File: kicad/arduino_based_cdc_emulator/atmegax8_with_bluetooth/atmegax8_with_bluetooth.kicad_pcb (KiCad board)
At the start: 2 copper layers, 110.5 x 172.6 mm, 70 parts, among them IC1 ATMEGA88-A, P1 CONN_9, P2 SPI, P3 CONN_4, Q1 BC817-40, U1 78L05, U2 F-6188, U3 LM358, Y1 Crystal_GND2

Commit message: update
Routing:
- net TX: track 2.51 -> 29.2 mm, vias 0 -> 1
- net RX: track 0.00 -> 23.3 mm, vias 0 -> 1
- net /LED2: track 0.00 -> 15.7 mm, vias 0 -> 2
- net /LED1: track 12.5 -> 17.3 mm, vias 0 -> 2
- net /ARESET: track 31.2 -> 26.7 mm
- net /MIC_BIAS: track 43.7 -> 39.7 mm
- net /MICP: track 44.9 -> 41.6 mm
- net GNDA: track 58.8 -> 55.8 mm
- net /MICN: track 39.3 -> 36.8 mm
- net GND: track 106.1 -> 103.9 mm, vias 4 -> 5
- net +5V: track 70.5 -> 68.5 mm
- net +BATT: track 60.1 -> 58.3 mm, vias 2 -> 1
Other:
- board size 110.5 x 172.6 mm -> 40.9 x 35.7 mm
- net class Default: trace_width 0.3 -> 0.15; via_dia 0.8 -> 0.5; via_drill 0.5 -> 0.3
- rule trace_min: 0.2032 -> 0.127
- rule via_min_drill: 0.5 -> 0.2
- rule via_min_size: 0.5 -> 0.45

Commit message: update
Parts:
- moved C28 7.52 mm to (93.7, 149.1)
- moved C23 5.39 mm to (79.8, 150.1), turned to 180 degrees
- moved R27 4.82 mm to (79.7, 146.1)
- moved C22 3.62 mm to (80.5, 143.0), turned to 180 degrees
- moved C26 3.02 mm to (79.7, 148.1), turned to 0 degrees
- moved Y1 2.77 mm to (84.3, 166.2)
- moved R6 2.53 mm to (86.9, 165.3)
- moved R5 2.20 mm to (89.4, 165.1)
- moved R20 2.19 mm to (79.8, 152.4)
- moved C16 1.84 mm to (80.0, 166.1)
- moved R23 1.81 mm to (80.1, 168.4)
- moved R18 1.79 mm to (80.1, 163.8)
- moved R2 1.78 mm to (102.6, 152.1)
- moved R8 1.56 mm to (80.1, 161.5)
- moved R21 1.30 mm to (80.0, 159.3)
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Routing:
- net Net-(C17-Pad1): track 24.2 -> 15.4 mm, vias 1 -> 2
- net /MIC_IN2: track 6.42 -> 14.5 mm
- net /MICP: track 41.6 -> 34.5 mm
- net GND: track 103.9 -> 97.8 mm, vias 5 -> 6
- net /LED2: track 15.7 -> 21.2 mm
- net Net-(C18-Pad1): track 21.7 -> 17.1 mm, vias 1 -> 2
- net Net-(C15-Pad2): track 12.6 -> 16.7 mm
- net /ARESET: track 26.7 -> 30.7 mm
- net Net-(C15-Pad1): track 13.6 -> 17.1 mm
- net /MICN: track 36.8 -> 40.1 mm
- net /LED1: track 17.3 -> 20.5 mm
- net TX: track 29.2 -> 31.4 mm
- net RX: track 23.3 -> 25.5 mm
- net Net-(IC1-Pad8): track 2.04 -> 4.18 mm
- net Net-(C14-Pad1): track 9.36 -> 11.4 mm
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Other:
- board size 40.9 x 35.7 mm -> 41.4 x 36.1 mm
- net class Default: clearance 0.2 -> 0.15; via_dia 0.5 -> 0.6; via_drill 0.3 -> 0.4
- rule trace_clearance: 0.2 -> 0.15

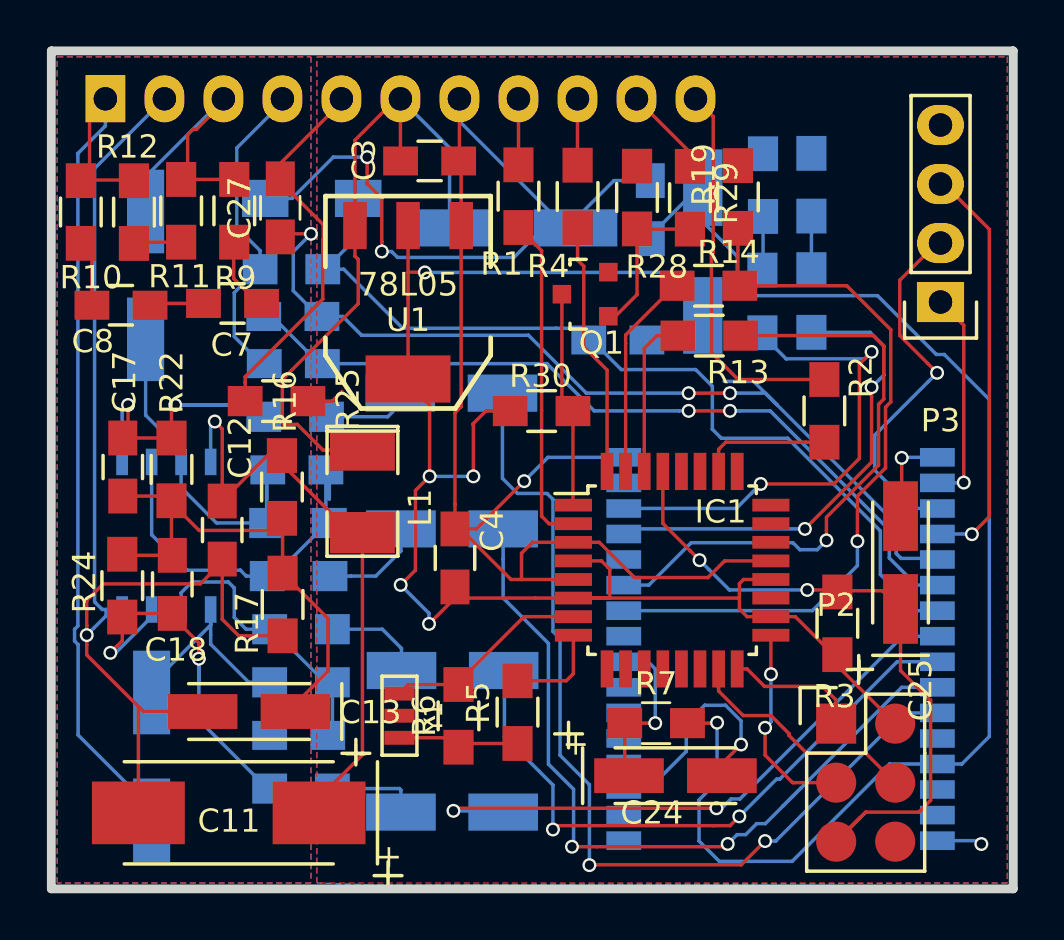
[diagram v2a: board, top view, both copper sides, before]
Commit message: changes to bt version, but it is not good, do not use this setup
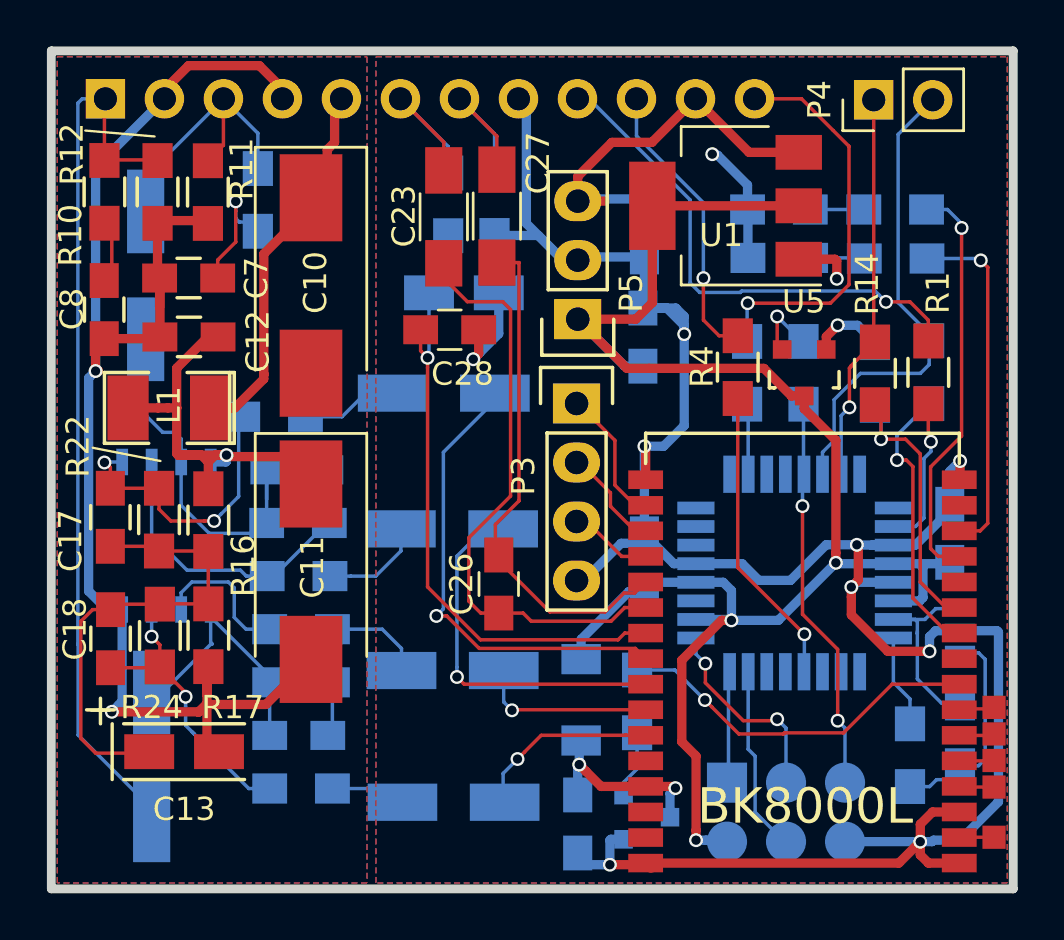
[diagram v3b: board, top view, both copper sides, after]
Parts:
- removed C25: 2u1, Capacitors_Tantalum_SMD:TantalC_SizeA_EIA-3216_HandSoldering
- removed Q1: BC817-40, TO_SOT_Packages_SMD:SOT-23
- removed R28: 47k, Resistors_SMD:R_0805_HandSoldering
- removed R29, R30: 10k, Resistors_SMD:R_0805_HandSoldering
- added C1: 100n, Capacitors_SMD:C_0805_HandSoldering, B.Cu at (94.9, 158.7)
- added J1: Ant, modules:1pin_smd, F.Cu at (109.9, 170.5)
- added J2: TMS, modules:1pin_smd, F.Cu at (109.9, 168.3)
- added J3: TCK, modules:1pin_smd, F.Cu at (109.9, 167.2)
- added J4: TDO, modules:1pin_smd, F.Cu at (109.9, 166.1)
- added J5: TDI, modules:1pin_smd, F.Cu at (109.9, 164.9)
- added P4: SERIAL, Pin_Headers:Pin_Header_Straight_1x02_Pitch2.54mm, F.Cu at (104.7, 138.8)
- added P5: CONN_4, Pin_Headers.pretty:Pin_Header_Straight_1x03, F.Cu at (92.0, 148.2)
- added U4: MAX809, TO_SOT_Packages_SMD.pretty:SOT-23, B.Cu at (95.0, 169.6)
- added U5: MAX809, TO_SOT_Packages_SMD.pretty:SOT-23, F.Cu at (101.7, 150.5)
- C10: value 100m/25V -> 100u/16V; footprint Capacitors_SMD:c_elec_6.3x7.7 -> Capacitors_Tantalum_SMD:CP_Tantalum_Case-D_EIA-7343-31_Hand; moved to F.Cu
- C11: value 47m/25V -> 100u/16V; footprint Capacitors_Tantalum_SMD:TantalC_SizeD_EIA-7343_HandSoldering -> Capacitors_Tantalum_SMD:CP_Tantalum_Case-D_EIA-7343-31_Hand
- C13: value 2m2/16V -> 4u7/10V; footprint Capacitors_Tantalum_SMD:TantalC_SizeA_EIA-3216_HandSoldering -> Capacitors_Tantalum_SMD.pretty:TantalC_SizeA_EIA-3216_Wave
- C14, C9: value 47m/25V -> 4.7m/25V
- C19: value 10m/16V -> 1m/16V
- C20, C21, C6: value 10m/16V -> 1m/16V; footprint Capacitors_SMD:c_elec_5x5.8 -> Capacitors_SMD:CP_Elec_5x5.8
- C22: footprint Capacitors_SMD:C_1206_HandSoldering -> Capacitors_Tantalum_SMD.pretty:TantalC_SizeA_EIA-3216_Wave
- C23: footprint Capacitors_SMD:C_0805_HandSoldering -> Capacitors_SMD:C_1206_HandSoldering; moved to F.Cu
- C24: value 2u2 -> 100n; footprint Capacitors_Tantalum_SMD:TantalC_SizeA_EIA-3216_HandSoldering -> Capacitors_SMD:C_0805_HandSoldering; moved to B.Cu
- C26, C28, U2: moved to F.Cu
- C27: footprint Capacitors_SMD:C_0805_HandSoldering -> Capacitors_SMD:C_1206_HandSoldering
- C3, C4, IC1, P2, R6, R9: moved to B.Cu
- D1: footprint Diodes_SMD:MiniMELF_Handsoldering -> Diodes_SMD:D_MiniMELF
- P1: value CONN_9 -> CONN_10; footprint Pin_Headers:Pin_Header_Straight_1x11 -> Pin_Headers:Pin_Header_Straight_1x12_Pitch2.54mm
- R1, R4: value 3k3 -> 1k
- R13: value 330 -> 1k; moved to B.Cu
- R14: value 330 -> 1k
- R19: value 4k7 -> 2k; moved to B.Cu
- R2, R3, R7: value 3k3 -> 1k; moved to B.Cu
- R25: value 1k2 -> 1k; moved to B.Cu
- R27: value 1k2 -> 1k
- R5: value 27 -> 100; moved to B.Cu
- U1: value 78L05 -> AP1117; footprint my_modules:SOT-223-REGULATOR -> TO_SOT_Packages_SMD:SOT-223-3_TabPin2
- U3: value LM358 -> TL072
- Y1: value Crystal_GND2 -> 16MHz; moved to B.Cu
- moved C5 26.6 mm to (92.0, 169.9), turned to -90 degrees
- moved Y1 24.4 mm to (108.5, 162.6)
- moved R6 21.6 mm to (108.5, 166.1)
- moved C4 21.3 mm to (108.0, 157.4)
- moved D1 20.0 mm to (92.1, 164.6), turned to 90 degrees
- moved R1 19.2 mm to (107.1, 150.5)
- moved C24 18.9 mm to (94.8, 149.0), turned to 90 degrees
- moved R5 17.0 mm to (106.3, 167.0)
- moved P3 16.3 mm to (91.9, 151.8), turned to 0 degrees
- moved C26 14.5 mm to (88.6, 159.6), turned to 90 degrees
- moved U2 14.5 mm to (108.4, 153.1), turned to 180 degrees
- moved U1 14.3 mm to (98.4, 143.3)
- moved R25 12.6 mm to (88.4, 143.2), turned to 90 degrees
- moved C11 11.0 mm to (80.5, 159.1), turned to -90 degrees
- moved R3 10.9 mm to (101.7, 150.5)
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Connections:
- C10 pad 2: GND -> GNDA
- C19 pad 2: /BTOUTRN -> /BTOUTLN
- C20 pad 1: /BTOUTR -> /BTOUTL
- C21 pad 2: /BTOUTLN -> /BTOUTRN
- C24 pad 1: /BT_RESET -> +5V
- C3 pad 1: +12V -> /CDC_ENA_12V
- C6 pad 1: /BTOUTL -> /BTOUTR
- IC1 pad 1: /CDC_ENA_5V -> (no net)
- IC1 pad 12: (no net) -> Net-(IC1-Pad12)
- IC1 pad 32: Net-(IC1-Pad32) -> (no net)
- P1 pad 10: /CDC_ENA_12V -> /DataOut
- P1 pad 11: Net-(P1-Pad11) -> /CDC_ENA_12V
- P1 pad 4: /MIC_IN2 -> GNDA
- P1 pad 5: /MIC_IN1 -> +12V
- P1 pad 6: +12V -> /MIC_IN2
- P1 pad 7: GND -> /MIC_IN1
- P1 pad 8: Net-(P1-Pad8) -> GND
- P1 pad 9: /DataOut -> Net-(P1-Pad9)
- R1 pad 1: Net-(P1-Pad8) -> Net-(P1-Pad9)
- R13 pad 2: RX -> TX
- R14 pad 2: TX -> RX
- R19 pad 1: TX -> RX
- R2 pad 1: Net-(P1-Pad11) -> Net-(P1-Pad12)
- R3 pad 1: /ARESET -> Net-(R3-Pad1)
- R3 pad 2: +5V -> /ARESET
- R4 pad 1: Net-(IC1-Pad32) -> Net-(IC1-Pad12)
- R7 pad 1: /BT_RESET -> Net-(R7-Pad1)
- R7 pad 2: +BATT -> /BT_RESET
- U2 pad 2: (no net) -> Net-(J1-Pad1)
- U2 pad 4: (no net) -> Net-(J2-Pad1)
- U2 pad 5: (no net) -> Net-(J3-Pad1)
- U2 pad 6: (no net) -> Net-(J4-Pad1)
- U2 pad 7: (no net) -> Net-(J5-Pad1)
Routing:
- net +BATT: track 58.3 -> 8.32 mm, vias 1 -> 2
- net /BTOUTRN: track 39.9 -> 9.06 mm, vias 2 -> 1
- net GND: track 97.8 -> 124.8 mm, vias 6 -> 12
- net /BTOUTR: track 34.5 -> 8.48 mm, vias 2 -> 1
- net Net-(P1-Pad9): track 0.00 -> 22.1 mm, vias 0 -> 1
- net TX: track 31.4 -> 12.1 mm
- net /MICN: track 40.1 -> 22.5 mm, vias 3 -> 0
- net Net-(P1-Pad11): track 17.4 -> 0.00 mm
- net Net-(P1-Pad12): track 0.00 -> 17.2 mm, vias 0 -> 1
- net /CDC_ENA_12V: track 3.86 -> 18.3 mm
- net /INL: track 17.8 -> 3.60 mm, vias 1 -> 0
- net Net-(IC1-Pad30): track 6.97 -> 21.0 mm
- net Net-(IC1-Pad12): track 0.00 -> 13.0 mm, vias 0 -> 1
- net RX: track 25.5 -> 12.8 mm
- net /ARESET: track 30.7 -> 18.3 mm
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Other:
- net class POWER added: clearance 0.15, trace_width 0.4, via_dia 0.6, via_drill 0.4
- board text added: "BK8000L"
- board text added: "MISO"
